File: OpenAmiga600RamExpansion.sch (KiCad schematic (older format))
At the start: 20 parts, among them J1 Conn_01x02, U1 NEC_424260, U2 NEC_424260, U3 MSM6242B

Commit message: Fix error in RTC power circuit
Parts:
- added J99: OSHW_LOGO, w_logo:Logo_copper_OSHW_6x6mm, symbol Conn_01x01
- BT1: footprint (none) -> OpenAmiga600RamExpansion:Battery_Holder_Coin_2032_BS-7
- C1, C2, C3, C4, C5, C6, C7: footprint (none) -> Capacitors_SMD:C_0805_HandSoldering
- C8: footprint (none) -> Capacitors_SMD:C_1206_HandSoldering
- CONN1: footprint MODULE -> OpenAmiga600RamExpansion:4UCON_10156_90deg
- D1: footprint (none) -> smd_trans:sot23
- J1: footprint (none) -> Pin_Headers:Pin_Header_Straight_1x02_Pitch2.54mm
- R1: renamed from R3; footprint (none) -> Resistors_SMD:R_0805_HandSoldering
- R2: renamed from R1; footprint (none) -> Resistors_SMD:R_0805_HandSoldering
- R3: renamed from R2; footprint (none) -> Resistors_SMD:R_0805_HandSoldering
- R4, R5: footprint (none) -> Resistors_SMD:R_0805_HandSoldering
- U1: renamed from U2; footprint MODULE -> OpenAmiga600RamExpansion:SOJ-40-Socket-LongPads
- U2: renamed from U1; footprint MODULE -> OpenAmiga600RamExpansion:SOJ-40-Socket-LongPads
- U3: footprint MODULE -> Housings_DIP:DIP-18_W7.62mm_Socket
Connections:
- net labels added: VDD
- wire segments 246 -> 211
- no-connect marks 40 -> 42

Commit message: Reposition some RTC components
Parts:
- J1: footprint Pin_Headers:Pin_Header_Straight_1x02_Pitch2.54mm -> OpenAmiga600RamExpansion:Pin_Header_Straight_1x02-ModSilkS
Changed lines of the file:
@@
 Sheet 1 1
 Title "OpenAmiga600RamExpansion"
-Date "2018-06-22"
-Rev "1git"
+Date "2018-06-26"
+Rev "1"
 Comp "SukkoPera"
 Comment1 ""
@@
 F 0 "J1" H 7925 2800 50  0000 C CNN
 F 1 "Conn_01x02" H 7925 2500 50  0001 C CNN
-F 2 "Pin_Headers:Pin_Header_Straight_1x02_Pitch2.54mm" H 7925 2700 50  0001 C CNN
+F 2 "OpenAmiga600RamExpansion:Pin_Header_Straight_1x02-ModSilkS" H 7925 2700 50  0001 C CNN
 F 3 "" H 7925 2700 50  0001 C CNN
 	1    7925 2700

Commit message: Minor silkscreen fixes
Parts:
- renumbered R3 to R1, R1 to R3, R5 to R4, R4 to R5
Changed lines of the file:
@@
 $EndComp
 $Comp
-L R R1
+L R R3
 U 1 1 5B285A9F
 P 8650 2000
-F 0 "R1" V 8730 2000 50  0000 C CNN
+F 0 "R3" V 8730 2000 50  0000 C CNN
 F 1 "10k" V 8650 2000 50  0000 C CNN
 F 2 "Resistors_SMD:R_0805_HandSoldering" V 8580 2000 50  0001 C CNN
@@
 $EndComp
 $Comp
-L R R3
+L R R1
 U 1 1 5B285ACD
 P 8450 2000
-F 0 "R3" V 8530 2000 50  0000 C CNN
+F 0 "R1" V 8530 2000 50  0000 C CNN
 F 1 "10k" V 8450 2000 50  0000 C CNN
 F 2 "Resistors_SMD:R_0805_HandSoldering" V 8380 2000 50  0001 C CNN
@@
 $EndComp
 $Comp
-L R R4
+L R R5
 U 1 1 5B285B00
 P 10225 1700
-F 0 "R4" V 10305 1700 50  0000 C CNN
+F 0 "R5" V 10305 1700 50  0000 C CNN
 F 1 "220" V 10225 1700 50  0000 C CNN
 F 2 "Resistors_SMD:R_0805_HandSoldering" V 10155 1700 50  0001 C CNN
@@
 $EndComp
 $Comp
-L R R5
+L R R4
 U 1 1 5B285B8E
 P 10950 1700
-F 0 "R5" V 11030 1700 50  0000 C CNN
+F 0 "R4" V 11030 1700 50  0000 C CNN
 F 1 "220" V 10950 1700 50  0000 C CNN
 F 2 "Resistors_SMD:R_0805_HandSoldering" V 10880 1700 50  0001 C CNN

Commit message: The sweetest perfection ;)
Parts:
- added D2: LED, OpenAmiga600RamExpansion:LED_0805_HandSoldering_ModSilkS, symbol LED
- added R6: 1K, Resistors_SMD:R_0805_HandSoldering, symbol R
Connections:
- wire segments 211 -> 216
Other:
- note added: "Power LED"
- moved on the sheet: C1, C2, C3, C4, C5, C6, J99

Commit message: Use HandSoldering version of SOT-23 footprint
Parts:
- D1: footprint smd_trans:sot23 -> TO_SOT_Packages_SMD:SOT-23_Handsoldering
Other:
- note removed: "Required RAM Type is 4 Mbit (256k×16) 70-80 ns DRAM, e.g.:\n- Hitachi HM514260AJ8, HM514260JP8\n- NEC µPD424260\n- Samsung KM416C256BJ\n- Hyundai HY514260BJC"
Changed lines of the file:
@@
 F 0 "D1" H 10375 2000 50  0000 C CNN
 F 1 "BAT54C" H 10600 2175 50  0000 C CNN
-F 2 "smd_trans:sot23" H 10600 2075 50  0001 C CNN
+F 2 "TO_SOT_Packages_SMD:SOT-23_Handsoldering" H 10600 2075 50  0001 C CNN
 F 3 "" H 10600 2075 50  0001 C CNN
 	1    10600 2075
@@
 Text Notes 10650 2500 0    60   ~ 0
 BAT721C\nis also\nfine
-Text Notes 2525 7450 0    60   ~ 0
-Required RAM Type is 4 Mbit (256k×16) 70-80 ns DRAM, e.g.:\n- Hitachi HM514260AJ8, HM514260JP8\n- NEC µPD424260\n- Samsung KM416C256BJ\n- Hyundai HY514260BJC
 $Comp
 L VDD #PWR021

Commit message: Switch to KiCad 5
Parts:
- BT1: symbol Battery_Cell -> OpenAmiga600RamExpansion-rescue:Battery_Cell
- C1, C2, C3, C4, C5, C6, C7, C8: symbol C -> OpenAmiga600RamExpansion-rescue:C
- CONN1: symbol A600_TRAPDOOR -> A600_TRAPDOOR:A600_TRAPDOOR
- D1: symbol D_x2_KCom_AAK -> OpenAmiga600RamExpansion-rescue:D_x2_KCom_AAK
- J1: symbol Conn_01x02 -> OpenAmiga600RamExpansion-rescue:Conn_01x02
- J99: symbol Conn_01x01 -> OpenAmiga600RamExpansion-rescue:Conn_01x01
- L1: renamed from D2; symbol LED -> OpenAmiga600RamExpansion-rescue:LED
- R1, R2, R3, R4, R5, R6: symbol R -> OpenAmiga600RamExpansion-rescue:R
- U1, U2: symbol NEC_424260 -> NEC_424260:NEC_424260
- U3: symbol MSM6242B -> MSM6242B:MSM6242B
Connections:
- wire segments 216 -> 249

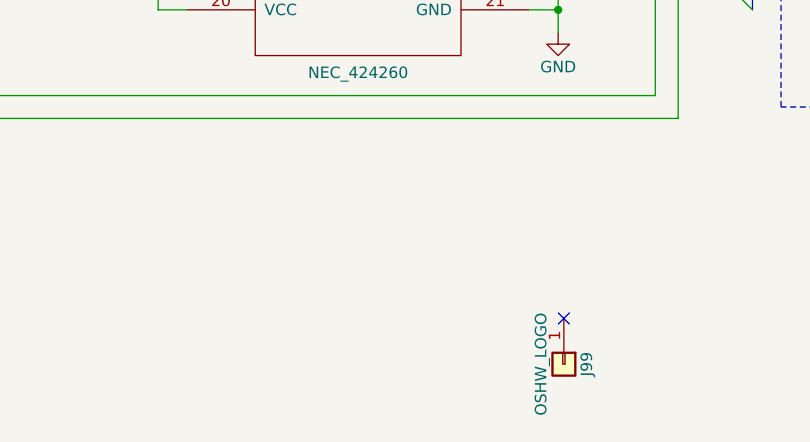
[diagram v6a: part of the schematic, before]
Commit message: Add (optional) decoupling electrolytic cap, just in case
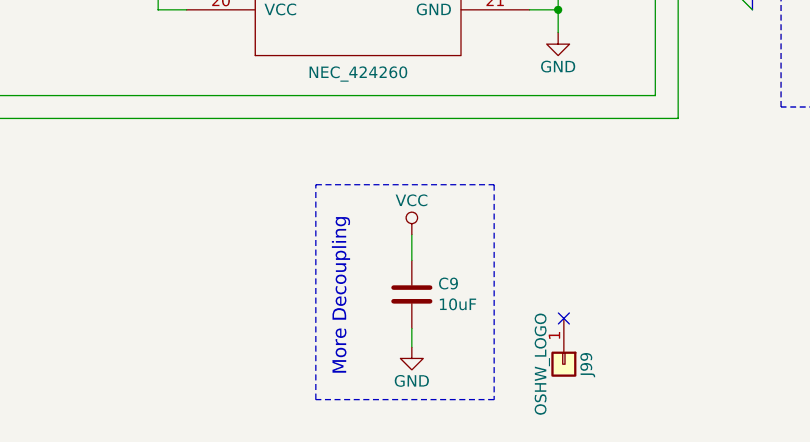
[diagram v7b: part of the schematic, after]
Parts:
- added C9: 10uF, Capacitor_THT:CP_Radial_D5.0mm_P2.00mm, symbol Device:C
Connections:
- wire segments 249 -> 251
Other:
- note added: "More Decoupling"
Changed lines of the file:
@@
 Wire Bus Line
 	950  675  7075 675
+$Comp
+L Device:C C9
+U 1 1 5B9B91C6
+P 6110 7220
+F 0 "C9" H 6225 7266 50  0000 L CNN
+F 1 "10uF" H 6225 7175 50  0000 L CNN
+F 2 "Capacitor_THT:CP_Radial_D5.0mm_P2.00mm" H 6148 7070 50  0001 C CNN
+F 3 "~" H 6110 7220 50  0001 C CNN
+	1    6110 7220
+	1    0    0    -1
+$EndComp
+$Comp
+L power:GND #PWR0101
+U 1 1 5B9B949A
+P 6110 7450
+F 0 "#PWR0101" H 6110 7200 50  0001 C CNN
+F 1 "GND" H 6110 7300 50  0000 C CNN
+F 2 "" H 6110 7450 50  0001 C CNN
+F 3 "" H 6110 7450 50  0001 C CNN
+	1    6110 7450
+	1    0    0    -1
+$EndComp
+$Comp
+L power:VCC #PWR0102
+U 1 1 5B9B960D
+P 6110 6960
+F 0 "#PWR0102" H 6110 6810 50  0001 C CNN
+F 1 "VCC" H 6110 7110 50  0000 C CNN
+F 2 "" H 6110 6960 50  0001 C CNN
+F 3 "" H 6110 6960 50  0001 C CNN
+	1    6110 6960
+	1    0    0    -1
+$EndComp
+Wire Wire Line
+	6110 7070 6110 6960
+Wire Wire Line
+	6110 7370 6110 7450
+Text Notes 5830 7580 1    60   ~ 0
+More Decoupling
+Wire Notes Line
+	5690 6740 6470 6740
+Wire Notes Line
+	6470 6740 6470 7680
+Wire Notes Line
+	6470 7680 5690 7680
+Wire Notes Line
+	5690 7680 5690 6740
+Wire Bus Line
+	850  800  850  3000
 Wire Bus Line
 	3600 800  3600 3100
 Wire Bus Line
-	850  800  850  3000
+	4425 800  4425 5775
+Wire Bus Line
+	7600 800  7600 5975
+Wire Bus Line
+	950  675  950  2400
 Wire Bus Line
 	3500 675  3500 2600
 Wire Bus Line
-	950  675  950  2400
-Wire Bus Line
-	7600 800  7600 5975
-Wire Bus Line
-	4425 800  4425 5775
+	7075 675  7075 5075
 Wire Bus Line
 	4725 675  4725 4875
-Wire Bus Line
-	7075 675  7075 5075
 $EndSCHEMATC
